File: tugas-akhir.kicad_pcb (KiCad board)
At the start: 2 copper layers, 120 x 100 mm, 34 parts, among them J1 Conn_01x02_Socket, J2 Conn_01x02_Pin (solenoid lini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, K1 Relay_SPDT, M1 Stepper_Motor_bipolar / Nema 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, M2 Stepper_Motor_bipolar / Nema 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, M3 Stepper_Motor_bipolar / Nema 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, Q1 2N3904, U1 ESP32-DEVKIT-V1, U2 DCDC_StepDown_LM2596, U3 TMC2208_SILENTSTEPSTICK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

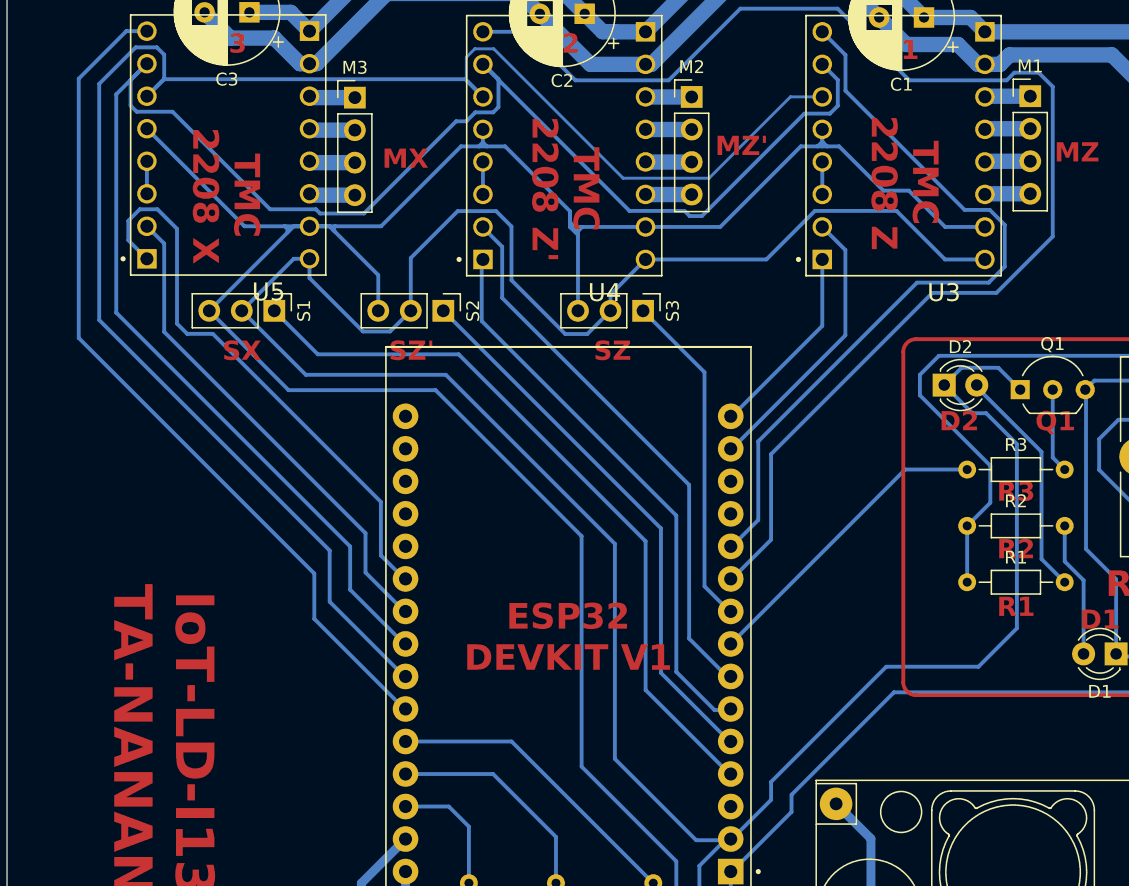
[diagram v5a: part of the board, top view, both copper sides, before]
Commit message: add reset button and refactor schematic
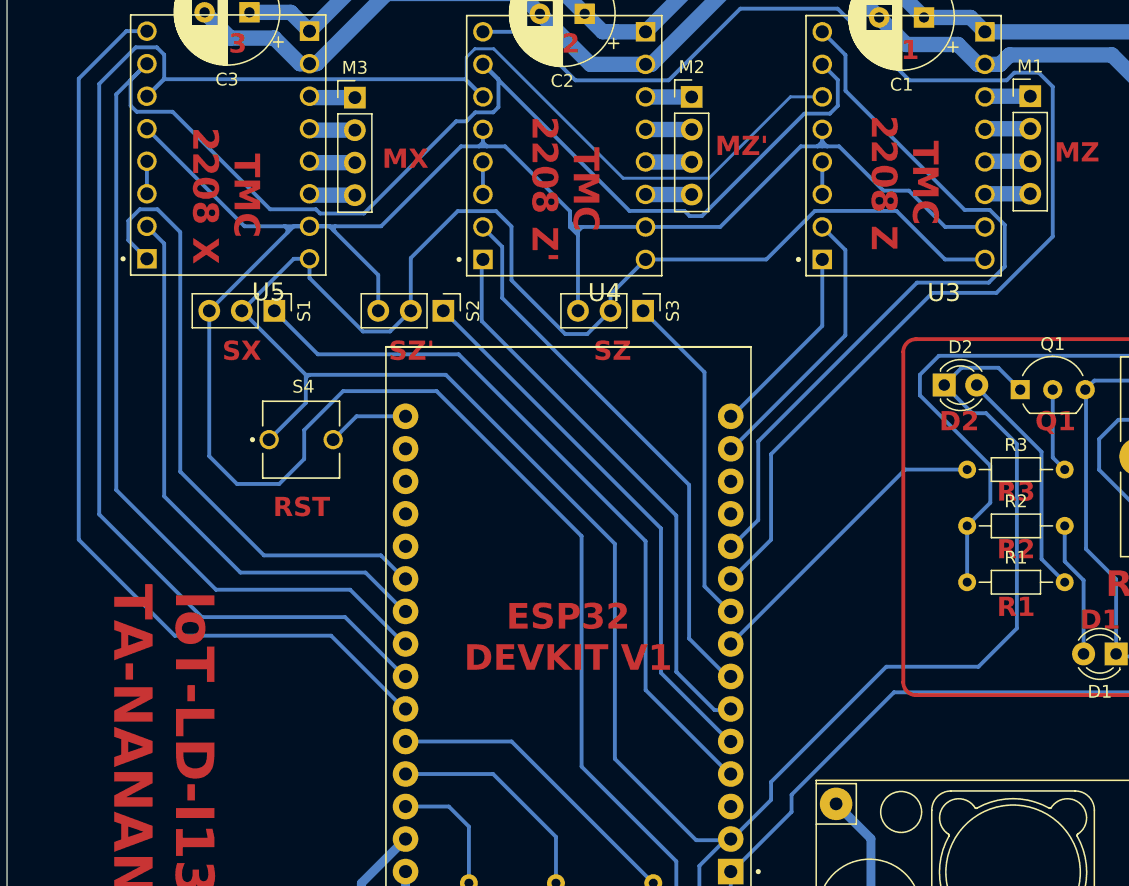
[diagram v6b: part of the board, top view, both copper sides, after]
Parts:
- added S4: BUTT-2, BUTT-2:SW_BUTT-2, F.Cu at (107.2, 83.0)
- J2: value Conn_01x02_Pin (solenoid linier) -> Conn_01x02_Pin (solenoid linear)
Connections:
- net +24V renamed V+
- net -24V renamed V-
- net Net-(D2-K) renamed GND
- net Net-(D3-K) renamed 3V3
- net Net-(U1-D12) renamed Z_LED
- net Net-(U1-D13) renamed ZP_LED
- net Net-(U1-D14) renamed X_LED
- net Net-(U1-D18) renamed Z_SW
- net Net-(U1-D19) renamed ZP_EN
- net Net-(U1-D2) renamed X_SW
- net Net-(U1-D21) renamed Z_EN
- net Net-(U1-D22) renamed Z_STEP
- net Net-(U1-D23) renamed Z_DIR
- net Net-(U1-D25) renamed MS1
- net Net-(U1-D26) renamed MS2
- net Net-(U1-D27) renamed X_EN
- net Net-(U1-D32) renamed X_DIR
- net Net-(U1-D33) renamed X_STEP
- net Net-(U1-D4) renamed ZP_SW
- net Net-(U1-D5) renamed RELAY
- net Net-(U1-RX2) renamed ZP_DIR
- net Net-(U1-TX2) renamed ZP_STEP
- U1 pad 16: unconnected-(U1-EN-Pad16) -> Net-(U1-EN)
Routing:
- net 3V3: track 380.1 -> 394.1 mm
- net X_EN: track 66.8 -> 73.9 mm
- net GND: track 238.7 -> 245.3 mm
- net MS2: track 132.5 -> 139.0 mm
- net Net-(U1-EN): track 0.00 -> 6.41 mm
- net MS1: track 139.0 -> 145.2 mm
- net X_STEP: track 38.5 -> 44.3 mm
- net X_DIR: track 44.4 -> 48.5 mm
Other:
- board text added: "RST"

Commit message: minor changes
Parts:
- S4: value BUTT-2 -> RESET BUTTON
- moved S4 40.6 mm to (106.8, 123.6), turned to 180 degrees
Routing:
- net Net-(U1-EN): track 6.41 -> 83.8 mm
- net Net-(U1-GND-Pad29): track 84.5 -> 111.1 mm
- net Net-(U1-VIN): track 53.8 -> 78.9 mm
- net GND: track 245.3 -> 260.3 mm
- net 3V3: track 394.1 -> 404.5 mm
- net X_EN: track 73.9 -> 68.7 mm
- net MS2: track 139.0 -> 135.7 mm
- net X_STEP: track 44.3 -> 41.7 mm
- net X_DIR: track 48.5 -> 46.3 mm
- net MS1: track 145.2 -> 143.0 mm
- net RELAY: track 24.1 -> 26.0 mm
- net ZP_DIR: track 44.0 -> 43.3 mm
